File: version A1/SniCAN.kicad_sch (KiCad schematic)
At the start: 102 parts, among them IC1 MIMXRT1062DVJ6B, J1 Conn_01x11_Male, J10 Screw_Terminal_01x02, J11 Screw_Terminal_01x02, J2 Conn_01x11_Male, J3 Conn_01x12_Male, J4 Conn_01x11_Male, J5 Conn_01x11_Male, J6 Conn_01x03_Male, J7 Conn_01x03_Male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

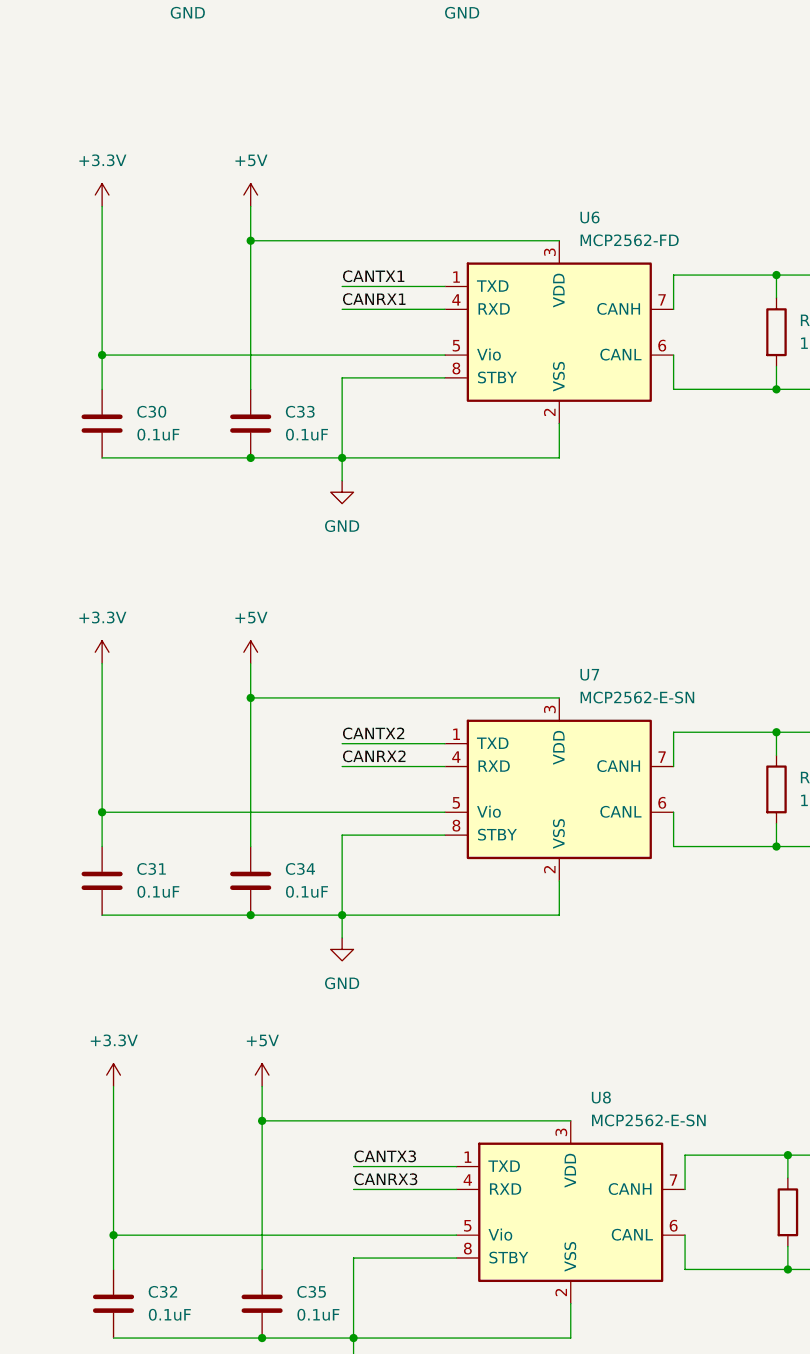
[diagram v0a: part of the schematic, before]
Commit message: colored pinout
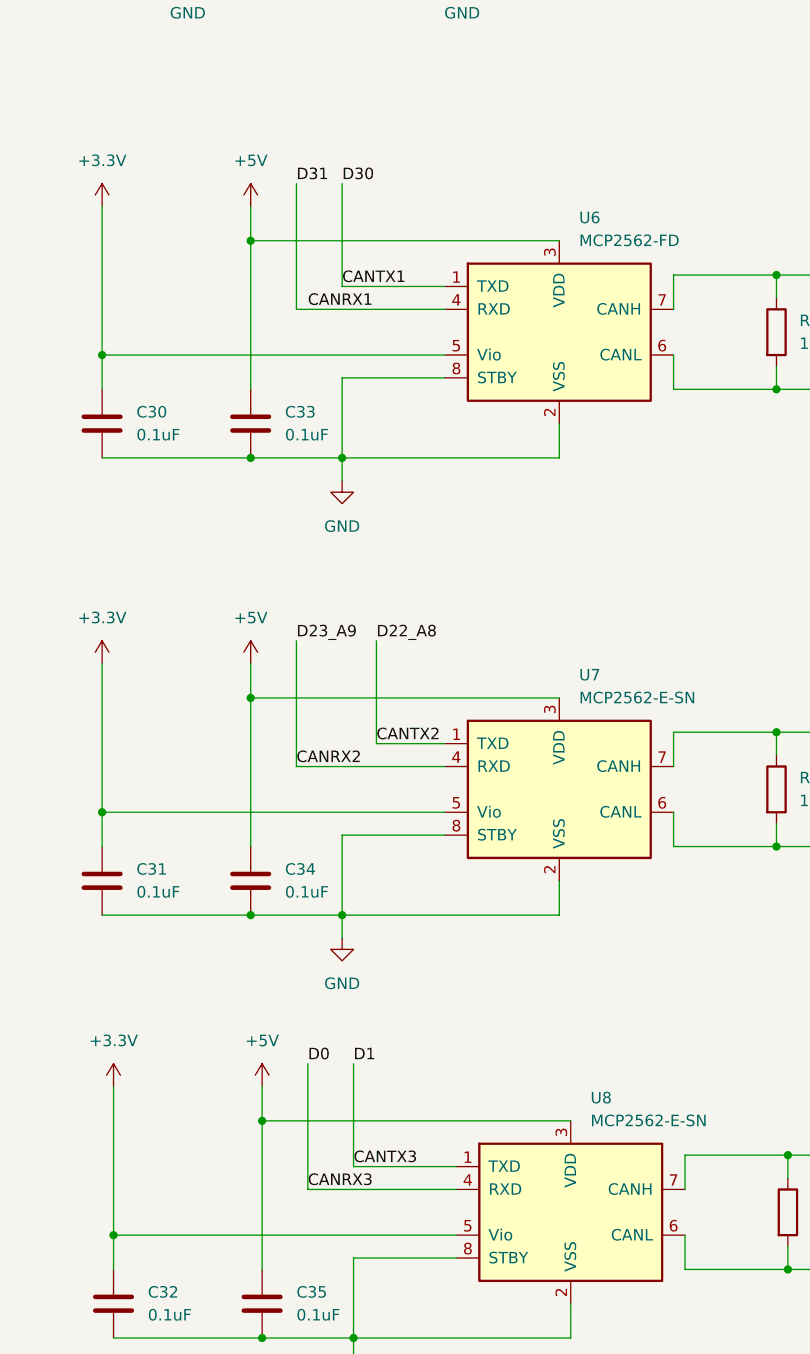
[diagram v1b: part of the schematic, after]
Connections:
- net D0 is gone; now on net CANRX3: IC1.G11 (GPIO_AD_B0_03), J3.11 (Pin_11)
- net D1 is gone; now on net CANTX3: IC1.M11 (GPIO_AD_B0_02), J5.9 (Pin_9)
- net D22_A8 is gone; now on net CANTX2: IC1.H13 (GPIO_AD_B1_08), J5.1 (Pin_1)
- net D23_A9 is gone; now on net CANRX2: IC1.M13 (GPIO_AD_B1_09), J5.5 (Pin_5)
- net D30 is gone; now on net CANTX1: IC1.E4 (GPIO_EMC_37), J2.8 (Pin_8)
- net D31 is gone; now on net CANRX1: IC1.C3 (GPIO_EMC_36), J2.3 (Pin_3)
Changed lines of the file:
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@@
   (junction (at 224.79 468.63) (diameter 0) (color 0 0 0 0)
   )
+  (junction (at 166.37 452.12) (diameter 0) (color 0 0 0 0)
+  )
   (junction (at 327.66 176.53) (diameter 0) (color 0 0 0 0)
   )
@@
   )
   (junction (at 248.92 33.02) (diameter 0) (color 0 0 0 0)
-  )
-  (junction (at 166.37 452.12) (diameter 0) (color 0 0 0 0)
   )
   (junction (at 224.79 455.93) (diameter 0) (color 0 0 0 0)
@@
     (stroke (width 0) (type default))
   )
+  (wire (pts (xy 180.34 445.77) (xy 180.34 457.2))
+    (stroke (width 0) (type default))
+  )
   (wire (pts (xy 98.425 323.85) (xy 98.425 328.295))
     (stroke (width 0) (type default))
@@
     (stroke (width 0) (type default))
   )
+  (wire (pts (xy 171.45 459.74) (xy 187.96 459.74))
+    (stroke (width 0) (type default))
+  )
   (wire (pts (xy 149.86 425.45) (xy 166.37 425.45))
     (stroke (width 0) (type default))
@@
     (stroke (width 0) (type default))
   )
+  (wire (pts (xy 177.8 504.19) (xy 189.23 504.19))
+    (stroke (width 0) (type default))
+  )
   (wire (pts (xy 112.395 40.64) (xy 120.015 40.64))
     (stroke (width 0) (type default))
@@
     (stroke (width 0) (type default))
   )
-  (wire (pts (xy 177.8 506.73) (xy 189.23 506.73))
-    (stroke (width 0) (type default))
-  )
   (wire (pts (xy 97.155 144.78) (xy 104.775 144.78))
     (stroke (width 0) (type default))
@@
     (stroke (width 0) (type default))
   )
+  (wire (pts (xy 171.45 445.77) (xy 171.45 459.74))
+    (stroke (width 0) (type default))
+  )
   (wire (pts (xy 60.325 328.295) (xy 60.325 332.74))
     (stroke (width 0) (type default))
@@
     (stroke (width 0) (type default))
   )
+  (wire (pts (xy 166.37 452.12) (xy 200.66 452.12))
+    (stroke (width 0) (type default))
+  )
   (wire (pts (xy 346.075 133.985) (xy 368.935 133.985))
     (stroke (width 0) (type default))
@@
     (stroke (width 0) (type default))
   )
-  (wire (pts (xy 176.53 457.2) (xy 187.96 457.2))
-    (stroke (width 0) (type default))
-  )
   (wire (pts (xy 104.775 94.615) (xy 113.665 94.615))
     (stroke (width 0) (type default))
@@
     (stroke (width 0) (type default))
   )
-  (wire (pts (xy 176.53 408.94) (xy 187.96 408.94))
+  (wire (pts (xy 171.45 408.94) (xy 187.96 408.94))
     (stroke (width 0) (type default))
   )
@@
     (stroke (width 0) (type default))
   )
-  (wire (pts (xy 176.53 459.74) (xy 187.96 459.74))
-    (stroke (width 0) (type default))
-  )
   (wire (pts (xy 346.075 49.53) (xy 368.935 49.53))
     (stroke (width 0) (type default))
@@
     (stroke (width 0) (type default))
   )
-  (wire (pts (xy 200.66 452.12) (xy 166.37 452.12))
-    (stroke (width 0) (type default))
-  )
   (wire (pts (xy 111.76 157.48) (xy 111.76 154.94))
     (stroke (width 0) (type default))
@@
     (stroke (width 0) (type default))
   )
+  (wire (pts (xy 180.34 457.2) (xy 187.96 457.2))
+    (stroke (width 0) (type default))
+  )
   (wire (pts (xy 187.96 467.36) (xy 176.53 467.36))
     (stroke (width 0) (type default))
@@
     (stroke (width 0) (type default))
   )
+  (wire (pts (xy 172.72 492.76) (xy 172.72 506.73))
+    (stroke (width 0) (type default))
+  )
   (wire (pts (xy 100.33 406.4) (xy 100.33 421.64))
     (stroke (width 0) (type default))
@@
     (stroke (width 0) (type default))
   )
+  (wire (pts (xy 176.53 394.97) (xy 176.53 406.4))
+    (stroke (width 0) (type default))
+  )
   (wire (pts (xy 360.68 186.055) (xy 368.935 186.055))
     (stroke (width 0) (type default))
@@
     (stroke (width 0) (type default))
   )
+  (wire (pts (xy 172.72 506.73) (xy 189.23 506.73))
+    (stroke (width 0) (type default))
+  )
   (wire (pts (xy 97.79 403.86) (xy 100.33 403.86))
     (stroke (width 0) (type default))
@@
     (stroke (width 0) (type default))
   )
+  (wire (pts (xy 177.8 492.76) (xy 177.8 504.19))
+    (stroke (width 0) (type default))
+  )
   (wire (pts (xy 44.45 421.64) (xy 60.96 421.64))
     (stroke (width 0) (type default))
@@
     (stroke (width 0) (type default))
   )
-  (wire (pts (xy 177.8 504.19) (xy 189.23 504.19))
+  (wire (pts (xy 171.45 394.97) (xy 171.45 408.94))
     (stroke (width 0) (type default))
   )
@@
     (effects (font (size 1.27 1.27)) (justify left bottom))
   )
+  (label "D1" (at 177.8 492.76 0) (fields_autoplaced)
+    (effects (font (size 1.27 1.27)) (justify left bottom))
+  )
   (label "D13" (at 348.615 106.68 0) (fields_autoplaced)
     (effects (font (size 1.27 1.27)) (justify left bottom))
@@
     (effects (font (size 1.27 1.27)) (justify left bottom))
   )
+  (label "D30" (at 176.53 394.97 0) (fields_autoplaced)
+    (effects (font (size 1.27 1.27)) (justify left bottom))
+  )
   (label "D45" (at 348.615 31.75 0) (fields_autoplaced)
     (effects (font (size 1.27 1.27)) (justify left bottom))
@@
     (effects (font (size 1.27 1.27)) (justify left bottom))
   )
+  (label "D31" (at 171.45 394.97 0) (fields_autoplaced)
+    (effects (font (size 1.27 1.27)) (justify left bottom))
+  )
   (label "POR_B" (at 75.565 338.455 0) (fields_autoplaced)
     (effects (font (size 1.27 1.27)) (justify left bottom))
@@
     (effects (font (size 1.27 1.27)) (justify left bottom))
   )
+  (label "D0" (at 172.72 492.76 0) (fields_autoplaced)
+    (effects (font (size 1.27 1.27)) (justify left bottom))
+  )
   (label "D32" (at 348.615 111.76 0) (fields_autoplaced)
     (effects (font (size 1.27 1.27)) (justify left bottom))
@@
     (effects (font (size 1.27 1.27)) (justify left bottom))
   )
+  (label "D22_A8" (at 180.34 445.77 0) (fields_autoplaced)
+    (effects (font (size 1.27 1.27)) (justify left bottom))
+  )
   (label "D15_A1" (at 348.615 175.895 0) (fields_autoplaced)
     (effects (font (size 1.27 1.27)) (justify left bottom))
@@
     (effects (font (size 1.27 1.27)) (justify left bottom))
   )
-  (label "CANRX2" (at 176.53 459.74 0) (fields_autoplaced)
+  (label "CANRX2" (at 171.45 459.74 0) (fields_autoplaced)
     (effects (font (size 1.27 1.27)) (justify left bottom))
   )
@@
     (effects (font (size 1.27 1.27)) (justify left bottom))
   )
-  (label "CANRX1" (at 176.53 408.94 0) (fields_autoplaced)
+  (label "CANRX1" (at 172.72 408.94 0) (fields_autoplaced)
     (effects (font (size 1.27 1.27)) (justify left bottom))
   )
@@
     (effects (font (size 1.27 1.27)) (justify left bottom))
   )
+  (label "D23_A9" (at 171.45 445.77 0) (fields_autoplaced)
+    (effects (font (size 1.27 1.27)) (justify left bottom))
+  )
   (label "D27_A13" (at 348.615 144.145 0) (fields_autoplaced)
     (effects (font (size 1.27 1.27)) (justify left bottom))
@@
     (effects (font (size 1.27 1.27)) (justify left bottom))
   )
-  (label "CANTX2" (at 176.53 457.2 0) (fields_autoplaced)
+  (label "CANTX2" (at 180.34 457.2 0) (fields_autoplaced)
     (effects (font (size 1.27 1.27)) (justify left bottom))
   )
@@
     (effects (font (size 1.27 1.27)) (justify left bottom))
   )
-  (label "CANRX3" (at 177.8 506.73 0) (fields_autoplaced)
-    (effects (font (size 1.27 1.27)) (justify left bottom))
-  )
+  (label "CANRX3" (at 172.72 506.73 0) (fields_autoplaced)
+    (effects (font (size 1.27 1.27)) (justify left bottom))
+  )
